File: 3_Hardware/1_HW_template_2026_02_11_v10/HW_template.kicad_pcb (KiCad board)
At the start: 2 copper layers, 63.5 x 118.1 mm, 47 parts, among them P1 type="R" model="Conn_01x32_Fe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, P2 type="R" model="Conn_01x32_Fe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, Q1 BSS316N, SW1 type="R" model="SW_Push" lib=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, U1 LD1117S33TR_SOT223, U2 SiP32508, U3 MCP6002/MCP6272, U4 MCP6002/MCP6272, Y1 Radar K-LC5-RFB-00C, Y2 OpenLog

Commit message: layout template
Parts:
- removed LED3: LEDred, LED_SMD:LED_1206_3216Metric_Pad1.42x1.75mm_HandSolder
- removed Q1: BSS316N, Package_TO_SOT_SMD:SOT-23
- removed R22: 100k, Resistor_SMD:R_0805_2012Metric_Pad1.20x1.40mm_HandSolder
- removed SD1: SD103AWS, Diode_SMD:D_SOD-323_HandSoldering
- removed SD2: SS13L, Diode_SMD:D_SMA
- removed SW1: type="R" model="SW_Push" lib="", Button_Switch_SMD:SW_SPST_PTS645
- removed the TP4 at (128.5, 42.5)
- added BZ1: Buzzer_Piezo, Buzzer_Beeper:Buzzer_Murata_PKMCS0909E, F.Cu at (175.2, 153.5)
- added C10: 100u, Capacitor_SMD:C_1210_3225Metric_Pad1.33x2.70mm_HandSolder, F.Cu at (137.3, 172.7)
- added C11: 4n7, Capacitor_SMD:C_0603_1608Metric_Pad1.08x0.95mm_HandSolder, F.Cu at (138.8, 176.2)
- added C12: 100u, Capacitor_SMD:C_1210_3225Metric_Pad1.33x2.70mm_HandSolder, F.Cu at (150.5, 174.0)
- added C13: 4n7, Capacitor_SMD:C_0603_1608Metric_Pad1.08x0.95mm_HandSolder, F.Cu at (149.0, 177.5)
- added C14: 10u, Capacitor_SMD:C_0603_1608Metric_Pad1.08x0.95mm_HandSolder, F.Cu at (154.0, 177.5)
- added C15: 10u, Capacitor_SMD:C_0805_2012Metric_Pad1.18x1.45mm_HandSolder, F.Cu at (172.0, 70.6)
- added C16: 100n, Capacitor_SMD:C_0805_2012Metric_Pad1.18x1.45mm_HandSolder, F.Cu at (141.0, 130.4)
- added C17: 10u, Capacitor_SMD:C_0805_2012Metric_Pad1.18x1.45mm_HandSolder, F.Cu at (134.5, 136.4)
- added C18: 100n, Capacitor_SMD:C_0805_2012Metric_Pad1.18x1.45mm_HandSolder, F.Cu at (172.0, 79.6)
- added C19: 100n, Capacitor_SMD:C_0805_2012Metric_Pad1.18x1.45mm_HandSolder, F.Cu at (142.0, 139.4)
- added C20: 10u, Capacitor_SMD:C_0805_2012Metric_Pad1.18x1.45mm_HandSolder, F.Cu at (158.0, 127.6)
- added C21: 100n, Capacitor_SMD:C_0805_2012Metric_Pad1.18x1.45mm_HandSolder, F.Cu at (156.0, 127.6)
- added C22: 10uF, Capacitor_SMD:C_0805_2012Metric_Pad1.18x1.45mm_HandSolder, F.Cu at (168.0, 127.6)
- added C23: 100n, Capacitor_SMD:C_0805_2012Metric_Pad1.18x1.45mm_HandSolder, F.Cu at (170.0, 127.6)
- added C7: 10u, Capacitor_SMD:C_0603_1608Metric_Pad1.08x0.95mm_HandSolder, F.Cu at (154.0, 158.0)
- added C8: 100n, Capacitor_SMD:C_0603_1608Metric_Pad1.08x0.95mm_HandSolder, F.Cu at (145.3, 174.2)
- added C9: 10u, Capacitor_SMD:C_0603_1608Metric_Pad1.08x0.95mm_HandSolder, F.Cu at (133.3, 177.7)
- added JP1: SolderJumper_2_Open, Jumper:SolderJumper-2_P1.3mm_Open_RoundedPad1.0x1.5mm, F.Cu at (157.8, 154.6)
- added JP2: SolderJumper_2_Open, Jumper:SolderJumper-2_P1.3mm_Open_RoundedPad1.0x1.5mm, F.Cu at (157.7, 174.2)
- added JP3: SolderJumper_2_Open, Jumper:SolderJumper-2_P1.3mm_Open_RoundedPad1.0x1.5mm, F.Cu at (173.0, 134.8)
- added TP1: Channel1, TestPoint:TestPoint_Loop_D2.60mm_Drill1.6mm_Beaded, F.Cu at (160.5, 71.6)
- added TP5: ~, TestPoint:TestPoint_Loop_D2.60mm_Drill1.6mm_Beaded, F.Cu at (160.5, 81.7)
- added TP6: ~, TestPoint:TestPoint_Loop_D2.60mm_Drill1.6mm_Beaded, F.Cu at (146.0, 134.4)
- added TP7: ~, TestPoint:TestPoint_Loop_D2.60mm_Drill1.6mm_Beaded, F.Cu at (157.0, 134.6)
- added TP8: ~, TestPoint:TestPoint_Loop_D2.60mm_Drill1.6mm_Beaded, F.Cu at (169.0, 134.8)
- C1: value 100uF -> 100n; footprint Capacitor_SMD:C_1206_3216Metric_Pad1.33x1.80mm_HandSolder -> Capacitor_SMD:C_0603_1608Metric_Pad1.08x0.95mm_HandSolder
- C2: value 10uF -> 10u; footprint Capacitor_SMD:C_0805_2012Metric_Pad1.18x1.45mm_HandSolder -> Capacitor_SMD:C_0603_1608Metric_Pad1.08x0.95mm_HandSolder
- C3: value 10uF -> 100u; footprint Capacitor_SMD:C_0805_2012Metric_Pad1.18x1.45mm_HandSolder -> Capacitor_SMD:C_1210_3225Metric_Pad1.33x2.70mm_HandSolder
- C4, C6: value 100n -> 4n7; footprint Capacitor_SMD:C_0805_2012Metric_Pad1.18x1.45mm_HandSolder -> Capacitor_SMD:C_0603_1608Metric_Pad1.08x0.95mm_HandSolder
- C5: value 100n -> 100u; footprint Capacitor_SMD:C_0805_2012Metric_Pad1.18x1.45mm_HandSolder -> Capacitor_SMD:C_1210_3225Metric_Pad1.33x2.70mm_HandSolder
- LED1: value LEDblue -> LEDred; footprint LED_SMD:LED_1206_3216Metric_Pad1.42x1.75mm_HandSolder -> LED_SMD:LED_0603_1608Metric_Pad1.05x0.95mm_HandSolder
- LED2: value LEDgreen -> LEDred; footprint LED_SMD:LED_1206_3216Metric_Pad1.42x1.75mm_HandSolder -> LED_SMD:LED_0603_1608Metric_Pad1.05x0.95mm_HandSolder
- R1: value 0R -> 100k; footprint Resistor_SMD:R_0805_2012Metric_Pad1.20x1.40mm_HandSolder -> Resistor_SMD:R_0603_1608Metric_Pad0.98x0.95mm_HandSolder
- R10, R14, R3: value 1k -> 10k; footprint Resistor_SMD:R_0805_2012Metric_Pad1.20x1.40mm_HandSolder -> Resistor_SMD:R_0603_1608Metric_Pad0.98x0.95mm_HandSolder
- R11, R2: value 1k -> 1M; footprint Resistor_SMD:R_0805_2012Metric_Pad1.20x1.40mm_HandSolder -> Resistor_SMD:R_0603_1608Metric_Pad0.98x0.95mm_HandSolder
- R12: footprint Resistor_SMD:R_0805_2012Metric_Pad1.20x1.40mm_HandSolder -> Resistor_SMD:R_0603_1608Metric_Pad0.98x0.95mm_HandSolder
- R13: value 12k -> 1k; footprint Resistor_SMD:R_0805_2012Metric_Pad1.20x1.40mm_HandSolder -> Resistor_SMD:R_0603_1608Metric_Pad0.98x0.95mm_HandSolder
- R15: value 1k -> 220R
- R16: value 22 -> 1k; footprint Resistor_SMD:R_0805_2012Metric_Pad1.20x1.40mm_HandSolder -> Resistor_SMD:R_0603_1608Metric_Pad0.98x0.95mm_HandSolder
- R17: value 47 -> 1k; footprint Resistor_SMD:R_0805_2012Metric_Pad1.20x1.40mm_HandSolder -> Resistor_SMD:R_0603_1608Metric_Pad0.98x0.95mm_HandSolder
- R18, R19: value 100 -> 10k
- R20: value 100 -> 100k
- R21: value 10 -> 1k
- R4: value ~ -> 1M; footprint Resistor_SMD:R_0805_2012Metric_Pad1.20x1.40mm_HandSolder -> Resistor_SMD:R_0603_1608Metric_Pad0.98x0.95mm_HandSolder
- R5, R7: value ~ -> 10k; footprint Resistor_SMD:R_0805_2012Metric_Pad1.20x1.40mm_HandSolder -> Resistor_SMD:R_0603_1608Metric_Pad0.98x0.95mm_HandSolder
- R6: value ~ -> 1k; footprint Resistor_SMD:R_0805_2012Metric_Pad1.20x1.40mm_HandSolder -> Resistor_SMD:R_0603_1608Metric_Pad0.98x0.95mm_HandSolder
- R8: value 10k -> 100k; footprint Resistor_SMD:R_0805_2012Metric_Pad1.20x1.40mm_HandSolder -> Resistor_SMD:R_0603_1608Metric_Pad0.98x0.95mm_HandSolder
- R9: value 12k -> 1M; footprint Resistor_SMD:R_0805_2012Metric_Pad1.20x1.40mm_HandSolder -> Resistor_SMD:R_0603_1608Metric_Pad0.98x0.95mm_HandSolder
- U1: value LD1117S33TR_SOT223 -> MCP6002-xSN; footprint Package_TO_SOT_SMD:SOT-223-3_TabPin2 -> Package_SO:SOIC-8_3.9x4.9mm_P1.27mm
- U2: value SiP32508 -> MCP6002-xSN; footprint Package_TO_SOT_SMD:TSOT-23-6_HandSoldering -> Package_SO:SOIC-8_3.9x4.9mm_P1.27mm
- U3: value MCP6002/MCP6272 -> MCP6002-xSN
- U4: value MCP6002/MCP6272 -> LD1117S33TR_SOT223; footprint Package_SO:SOIC-8_3.9x4.9mm_P1.27mm -> Package_TO_SOT_SMD:SOT-223-3_TabPin2
- Y1: value Radar K-LC5-RFB-00C -> OpenLog; footprint HW_template:Radar_K-LC5 -> Connector_PinHeader_2.54mm:PinHeader_1x06_P2.54mm_Vertical
- Y2: value OpenLog -> Radar K-LC5-RFB-00C; footprint Connector_PinHeader_2.54mm:PinHeader_1x06_P2.54mm_Vertical -> HW_template:Radar_K-LC5
- moved R1 132.2 mm to (133.6, 159.5), turned to 180 degrees
- moved U2 131.9 mm to (143.8, 177.8)
- moved U1 128.6 mm to (144.0, 158.1)
- moved R2 126.8 mm to (137.6, 156.5), turned to -90 degrees
- moved R8 126.8 mm to (133.3, 179.2), turned to 180 degrees
- moved C1 126.7 mm to (145.6, 154.5), turned to 180 degrees
- moved R12 125.2 mm to (152.0, 177.5), turned to 90 degrees
- moved R4 125.1 mm to (150.6, 158.0), turned to -90 degrees
- moved R3 123.7 mm to (136.1, 156.5), turned to 90 degrees
- moved R5 122.7 mm to (152.1, 158.0), turned to 90 degrees
- moved C2 121.6 mm to (133.6, 158.0), turned to 180 degrees
- moved R9 121.5 mm to (137.3, 176.2), turned to -90 degrees
- moved R17 120.0 mm to (197.5, 137.6), turned to 90 degrees
- moved R16 119.9 mm to (191.0, 137.6), turned to 90 degrees
- moved R11 119.7 mm to (150.5, 177.5), turned to -90 degrees
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- renumbered TP1 to TP2, TP2 to TP4
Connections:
- C1 pad 1: +5V -> 3V3_INT
- C2 pad 1: Net-(U1-VI) -> Net-(U1A-+)
- C2 pad 2: GND -> IF_Q
- C3 pad 1: Net-(U1-VO) -> Net-(C3-Pad1)
- C4 pad 1: 3V3_INT -> Net-(U1B-+)
- C4 pad 2: GND -> Net-(U1A--)
- C5 pad 1: 3V3_INT -> Net-(C5-Pad1)
- C6 pad 1: 3V3_INT -> Net-(JP1-A)
- C6 pad 2: GND -> Net-(U1B--)
- R1 pad 1: Net-(U1-VO) -> Net-(U1A-+)
- R1 pad 2: 3V3_INT -> Vref
- R10 pad 1: Net-(U3A--) -> Net-(U2A--)
- R10 pad 2: GND -> Net-(C10-Pad1)
- R11 pad 1: Net-(U3B--) -> Net-(JP2-A)
- R11 pad 2: GND -> Net-(U2B--)
- R12 pad 1: Net-(U4B-+) -> Net-(U2B--)
- R12 pad 2: Net-(U4A--) -> Net-(C12-Pad1)
- R13 pad 1: /channel2/out -> Net-(JP2-A)
- R13 pad 2: Net-(U4B--) -> PC1
- R14 pad 1: Net-(U4A--) -> PC1
- R15 pad 1: Net-(U4B--) -> Net-(BZ1-+)
- R15 pad 2: GND -> Buzz
- R16 pad 1: Enable -> D0
- R17 pad 1: Enable -> D1
- R18 pad 1: Enable -> 3V3_INT
- R18 pad 2: Net-(LED3-A) -> Net-(U3A-+)
- R19 pad 1: Enable -> Net-(U3A-+)
- R19 pad 2: Net-(SD1-A) -> GND
- R2 pad 1: Net-(U1-VI) -> Net-(U1B-+)
- R2 pad 2: GND -> Net-(U1A--)
- R20 pad 1: Enable -> PA5
- R20 pad 2: Net-(SD2-A) -> Net-(U3B-+)
- R21 pad 1: +5V -> Net-(JP3-A)
- R21 pad 2: Net-(Q1-D) -> GND
- R3 pad 1: Net-(U1-VO) -> Net-(U1A--)
- R3 pad 2: GND -> Net-(C3-Pad1)
- R4 pad 1: /channel1/out -> Net-(JP1-A)
- R4 pad 2: PC1 -> Net-(U1B--)
- R5 pad 1: PC1 -> Net-(U1B--)
- R5 pad 2: GND -> Net-(C5-Pad1)
- R6 pad 1: /channel2/out -> Net-(JP1-A)
- R8 pad 1: Net-(U3B-+) -> Net-(U2A-+)
- R8 pad 2: Net-(U3A--) -> Vref
- R9 pad 1: /channel1/out -> Net-(U2B-+)
- R9 pad 2: Net-(U3B--) -> Net-(U2A--)
- TP3 pad 1: GND -> PC3
- U1 pad 1: GND -> Net-(U1B-+)
- U1 pad 2: Net-(U1-VO) -> Net-(U1A--)
- U1 pad 3: Net-(U1-VI) -> Net-(U1A-+)
- U2 pad 1: Net-(U1-VI) -> Net-(U2B-+)
- U2 pad 2: Net-(U1-VI) -> Net-(U2A--)
- U2 pad 3: Enable -> Net-(U2A-+)
- U2 pad 5: +5V -> Net-(U2B-+)
- U2 pad 6: +5V -> Net-(U2B--)
- U3 pad 1: Net-(U3B-+) -> Vref
- U3 pad 2: Net-(U3A--) -> Vref
- U3 pad 3: /channel1/in -> Net-(U3A-+)
- U3 pad 6: Net-(U3B--) -> /Analog/VCO_in
- U3 pad 7: /channel1/out -> /Analog/VCO_in
- U4 pad 1: Net-(U4B-+) -> GND
- U4 pad 2: Net-(U4A--) -> Net-(JP3-A)
- U4 pad 3: /channel2/in -> +5V
- Y1 pad 1: unconnected-(Y1-IF_Q-Pad1) -> PE6
- Y1 pad 2: 3V3_INT -> PA9
- Y1 pad 3: unconnected-(Y1-IF_I-Pad3) -> PA10
- Y1 pad 4: GND -> +5V
- Y1 pad 5: PA5 -> GND
- Y2 pad 1: PE6 -> IF_Q
- Y2 pad 2: PA9 -> 3V3_INT
- Y2 pad 3: PA10 -> IF_I
- Y2 pad 4: +5V -> GND
- Y2 pad 5: GND -> /Analog/VCO_in
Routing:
- net Net-(JP3-A): track 0.00 -> 27.8 mm
- net Net-(JP2-A): track 0.00 -> 17.9 mm
- net Net-(JP1-A): track 0.00 -> 17.8 mm
- net Net-(U2B-+): track 0.00 -> 12.0 mm
- net Net-(U1B-+): track 0.00 -> 12.0 mm
- net +5V: track 0.00 -> 11.4 mm
- net Net-(U2A-+): track 0.00 -> 10.9 mm
- net Net-(U1A-+): track 0.00 -> 10.9 mm
- net /Analog/VCO_in: track 0.00 -> 7.51 mm
- net Net-(U3A-+): track 0.00 -> 6.68 mm
- net Net-(U2B--): track 0.00 -> 5.78 mm
- net 3V3_INT: track 0.00 -> 5.61 mm
- net Net-(U1B--): track 0.00 -> 5.61 mm
- net Net-(U2A--): track 0.00 -> 5.58 mm
- net Net-(U1A--): track 0.00 -> 5.58 mm
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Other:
- board text added: "+3V3"
- board text added: "+5V"
- board text added: "CH1 - IF_Q"
- board text added: "CH2 - IF_I"
- board text added: "D0 D1"
- board text added: "Debug"
- board text added: "IN"
- board text added: "OUT"
- board text added: "VREF"
- board text added: "bzzzzz"
- board text added: "err0: 0 0 err1: 0 1 err2: 1 0 err3: 1 1"

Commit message: added AD8232
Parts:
- C15, C18: footprint Capacitor_SMD:C_0805_2012Metric_Pad1.18x1.45mm_HandSolder -> Capacitor_SMD:C_0603_1608Metric_Pad1.08x0.95mm_HandSolder
- moved C15 4.42 mm to (174.1, 74.5)
- moved C18 3.37 mm to (174.1, 77.0)

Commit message: added datasheet and started layout
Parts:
- added C25: 1n, Capacitor_SMD:C_0603_1608Metric_Pad1.08x0.95mm_HandSolder, F.Cu at (145.4, 119.4)
- added C26: 330n, Capacitor_SMD:C_0603_1608Metric_Pad1.08x0.95mm_HandSolder, F.Cu at (145.4, 121.9)
- added C27: 330n, Capacitor_SMD:C_0603_1608Metric_Pad1.08x0.95mm_HandSolder, F.Cu at (145.4, 124.5)
- added C28: 100n, Capacitor_SMD:C_0603_1608Metric_Pad1.08x0.95mm_HandSolder, F.Cu at (145.4, 127.0)
- added C29: 100n, Capacitor_SMD:C_0603_1608Metric_Pad1.08x0.95mm_HandSolder, F.Cu at (145.4, 129.5)
- added C30: 1n5, Capacitor_SMD:C_0603_1608Metric_Pad1.08x0.95mm_HandSolder, F.Cu at (145.4, 132.0)
- added C31: 10n, Capacitor_SMD:C_0603_1608Metric_Pad1.08x0.95mm_HandSolder, F.Cu at (145.4, 134.5)
- added LA1: MountingHole_Pad, TestPoint:TestPoint_Loop_D2.60mm_Drill1.6mm_Beaded, F.Cu at (150.1, 120.7)
- added R23: 10M, Resistor_SMD:R_0805_2012Metric_Pad1.20x1.40mm_HandSolder, F.Cu at (155.0, 119.7)
- added R24: 10M, Resistor_SMD:R_0805_2012Metric_Pad1.20x1.40mm_HandSolder, F.Cu at (155.0, 122.6)
- added R25: 10M, Resistor_SMD:R_0805_2012Metric_Pad1.20x1.40mm_HandSolder, F.Cu at (155.0, 125.5)
- added R28: 1M4, Resistor_SMD:R_0805_2012Metric_Pad1.20x1.40mm_HandSolder, F.Cu at (155.0, 128.5)
- added R29: 180k, Resistor_SMD:R_0805_2012Metric_Pad1.20x1.40mm_HandSolder, F.Cu at (155.0, 131.4)
- added R30: 360k, Resistor_SMD:R_0805_2012Metric_Pad1.20x1.40mm_HandSolder, F.Cu at (159.8, 119.7)
- added R31: 100k, Resistor_SMD:R_0805_2012Metric_Pad1.20x1.40mm_HandSolder, F.Cu at (159.8, 122.6)
- added R34: 180k, Resistor_SMD:R_0805_2012Metric_Pad1.20x1.40mm_HandSolder, F.Cu at (159.8, 125.5)
- added R35: 10M, Resistor_SMD:R_0805_2012Metric_Pad1.20x1.40mm_HandSolder, F.Cu at (159.8, 128.5)
- added R36: 10M, Resistor_SMD:R_0805_2012Metric_Pad1.20x1.40mm_HandSolder, F.Cu at (159.8, 131.4)
- added R37: 10M, Resistor_SMD:R_0805_2012Metric_Pad1.20x1.40mm_HandSolder, F.Cu at (164.5, 119.7)
- added R38: 1M, Resistor_SMD:R_0805_2012Metric_Pad1.20x1.40mm_HandSolder, F.Cu at (164.5, 122.6)
- added R39: 1M, Resistor_SMD:R_0805_2012Metric_Pad1.20x1.40mm_HandSolder, F.Cu at (164.5, 125.5)
- added R40: 1M, Resistor_SMD:R_0805_2012Metric_Pad1.20x1.40mm_HandSolder, F.Cu at (164.5, 128.5)
- added RA1: MountingHole_Pad, TestPoint:TestPoint_Loop_D2.60mm_Drill1.6mm_Beaded, F.Cu at (150.1, 125.8)
- added RL1: MountingHole_Pad, TestPoint:TestPoint_Loop_D2.60mm_Drill1.6mm_Beaded, F.Cu at (150.1, 130.8)
- moved JP3 119.9 mm to (53.4, 127.8), turned to 180 degrees
- moved C18 117.8 mm to (57.0, 89.0), turned to 90 degrees
- moved C15 116.5 mm to (58.5, 89.0), turned to 90 degrees
- moved TP8 116.2 mm to (53.4, 123.8), turned to 180 degrees
- moved R21 112.0 mm to (60.5, 127.3), turned to 0 degrees
- moved C23 109.6 mm to (60.5, 124.8), turned to 0 degrees
- moved Y2 107.8 mm to (62.0, 94.1), turned to 180 degrees
- moved C22 107.6 mm to (60.5, 122.8), turned to 0 degrees
- moved TP7 106.0 mm to (53.5, 111.8), turned to 180 degrees
- moved U4 105.8 mm to (58.0, 117.8), turned to 180 degrees
- moved U2 100.2 mm to (79.3, 101.1)
- moved C10 100.2 mm to (72.8, 96.0)
- moved C11 100.2 mm to (74.3, 99.5)
- moved C12 100.2 mm to (86.0, 97.3)
- moved C13 100.2 mm to (84.5, 100.8)
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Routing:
- added copper zone on In2.Cu, net 3V3_INT
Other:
- copper layers 2 -> 4
- board text added: "ET.PM4 = Radar-Sensor perritho - grebnbog"
- board text removed: "Sensor-Board: HW template for ET.PM4 = Radar-Sensor (c) renn@zhaw.ch January 2026"
- board text removed: "The 32 pin connectors are on the bottom side!"
- board text removed: "The GND plates have already been added. Press B to fill, CTRL + B to unfill all plates/zones."

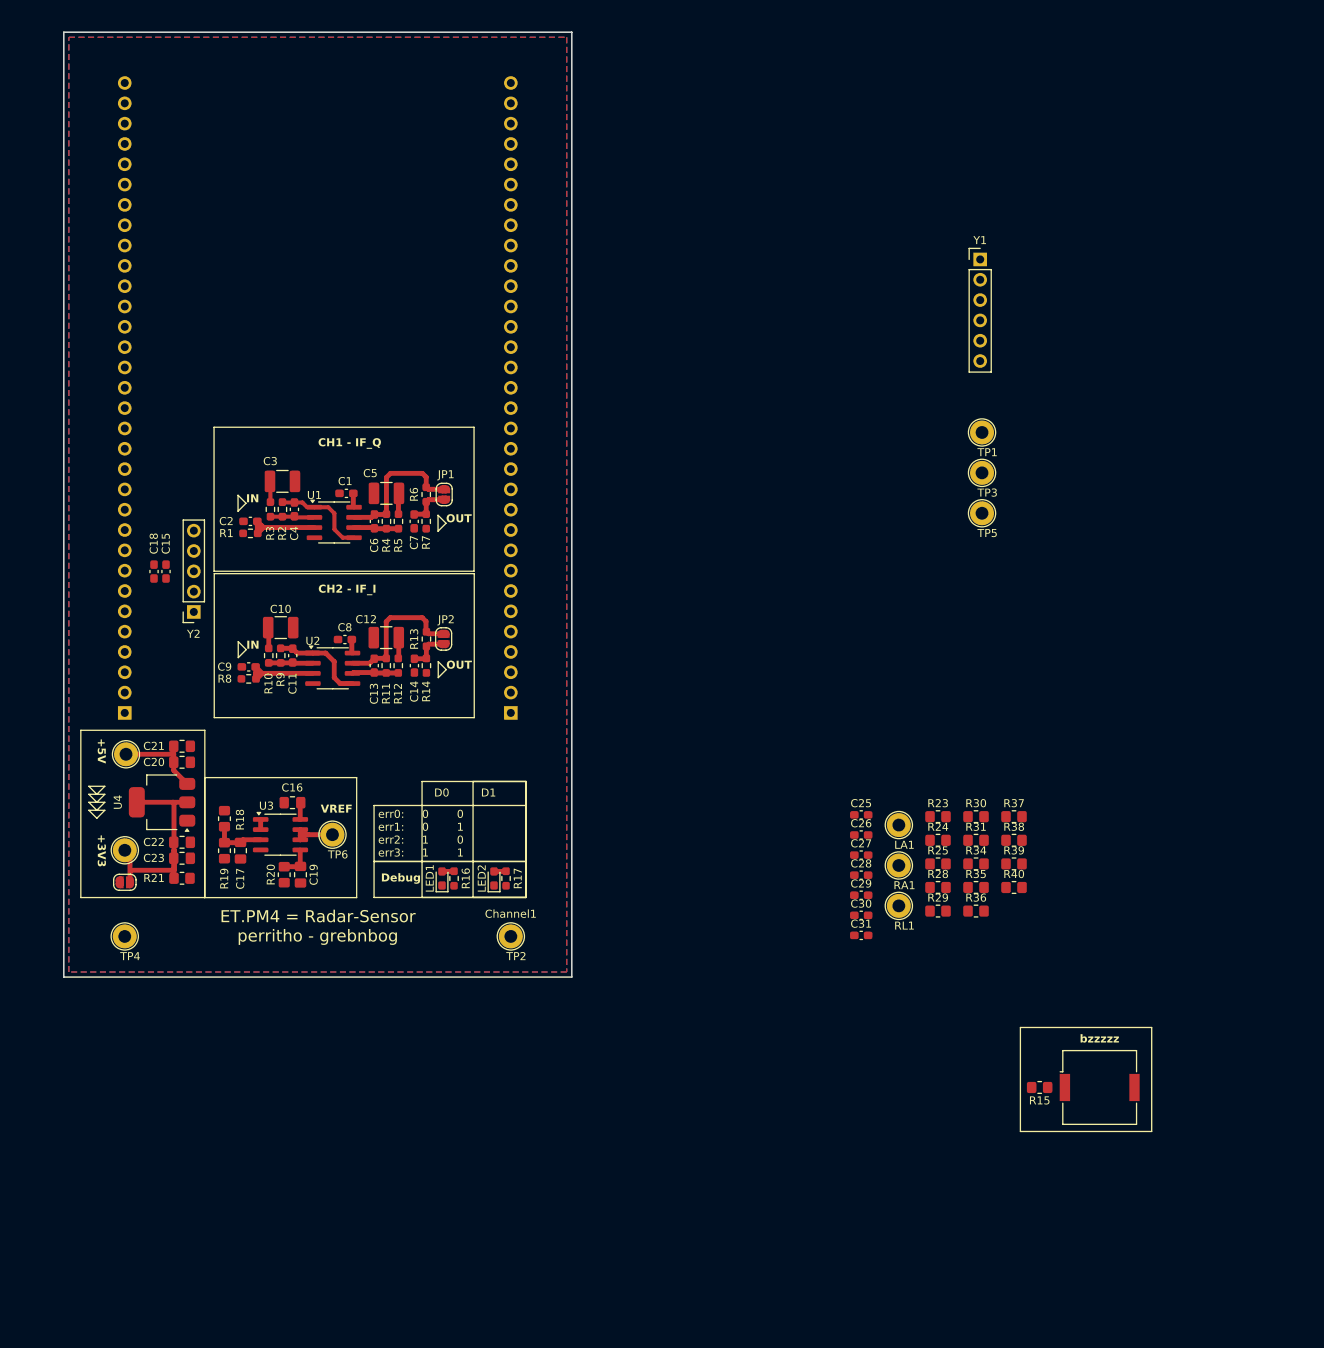
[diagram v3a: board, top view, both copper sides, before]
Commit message: updated layout
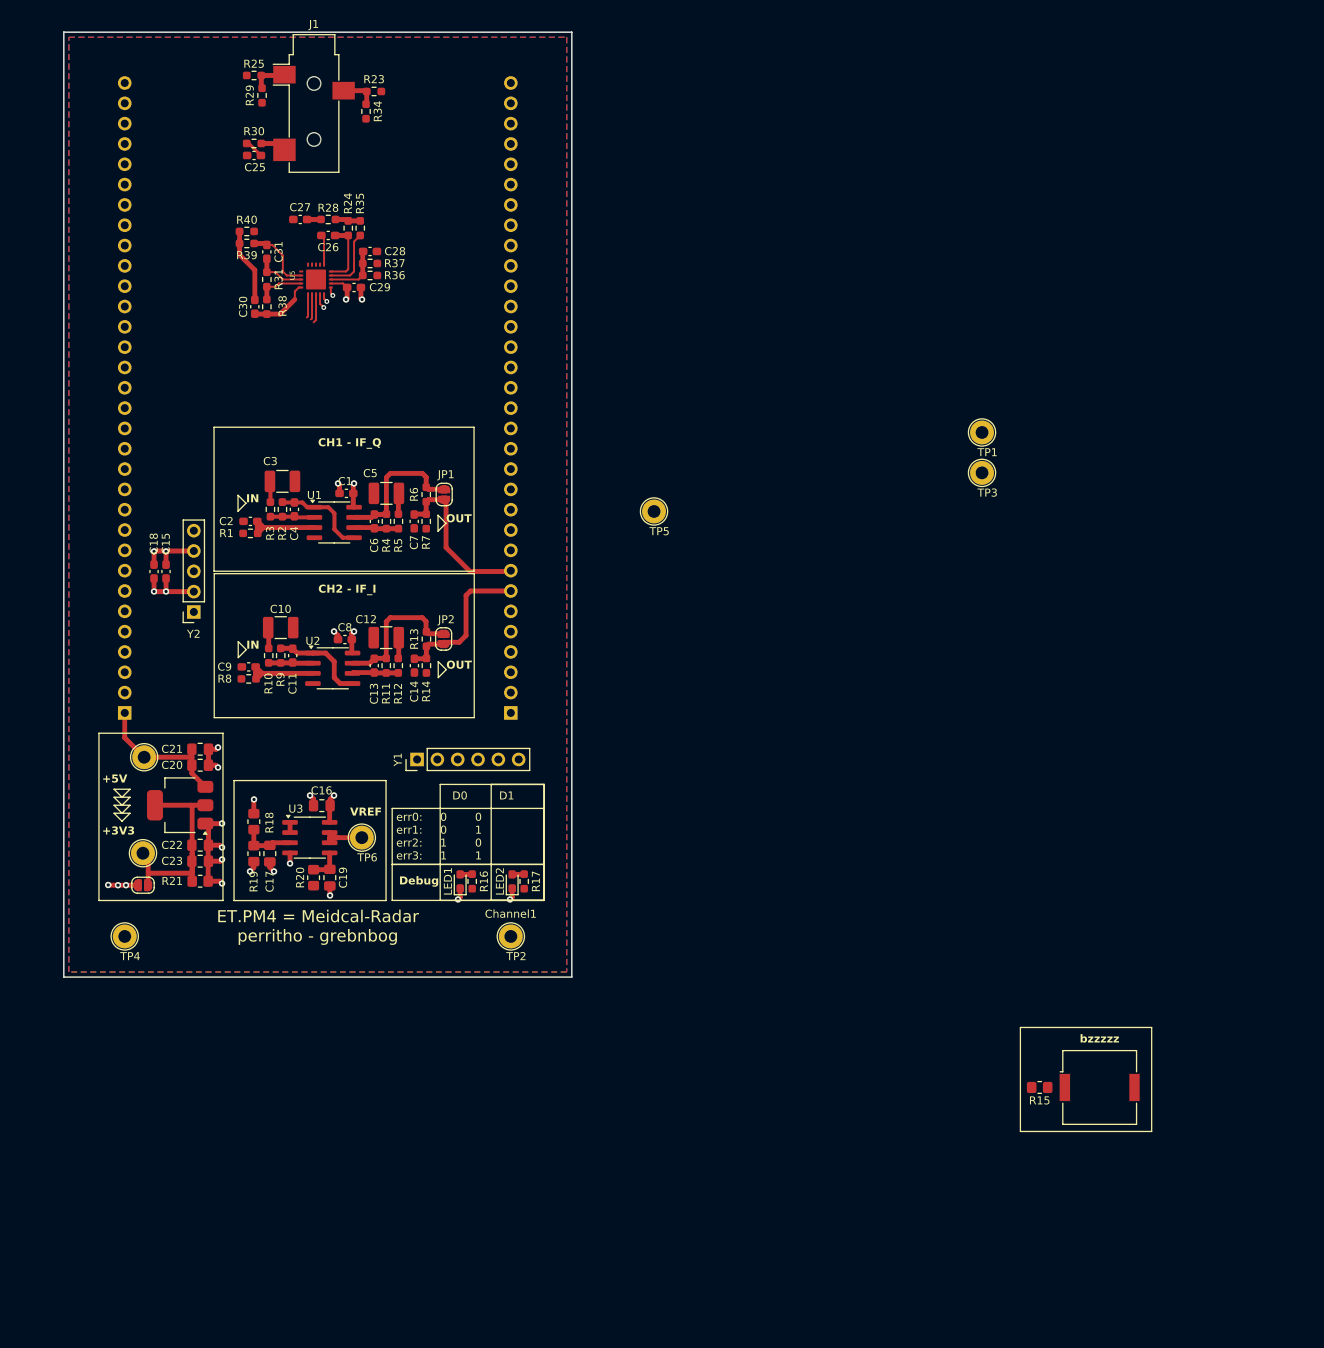
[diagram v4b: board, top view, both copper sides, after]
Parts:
- removed LA1, RA1, RL1: MountingHole_Pad, TestPoint:TestPoint_Loop_D2.60mm_Drill1.6mm_Beaded
- added J1: AudioJack3, Connector_Audio:Jack_3.5mm_CUI_SJ-3523-SMT_Horizontal, F.Cu at (77.0, 30.5)
- added U5: AD8232ACPZ-R7, AD8232:LFCSP_20, F.Cu at (77.2, 52.5)
- R23, R24, R25, R28, R29, R30, R31, R34, R35, R36, R37, R38, R39, R40: footprint Resistor_SMD:R_0805_2012Metric_Pad1.20x1.40mm_HandSolder -> Resistor_SMD:R_0603_1608Metric_Pad0.98x0.95mm_HandSolder
- moved R29 132.4 mm to (70.5, 29.5), turned to -90 degrees
- moved R25 130.5 mm to (69.5, 27.0)
- moved R40 126.2 mm to (68.6, 46.5)
- moved R30 123.4 mm to (69.5, 35.5), turned to 180 degrees
- moved R39 123.3 mm to (68.6, 48.0)
- moved R34 121.1 mm to (83.5, 31.5), turned to -90 degrees
- moved R23 114.8 mm to (84.5, 29.0), turned to 180 degrees
- moved R38 114.8 mm to (71.1, 55.9), turned to -90 degrees
- moved C31 113.2 mm to (71.1, 49.0), turned to 90 degrees
- moved R28 113.1 mm to (78.8, 45.0)
- moved R31 113.0 mm to (71.1, 52.5), turned to -90 degrees
- moved R35 112.8 mm to (82.8, 46.1), turned to 90 degrees
- moved C25 112.1 mm to (69.5, 37.0)
- moved R36 109.8 mm to (84.0, 52.0), turned to 180 degrees
- moved C30 107.4 mm to (69.6, 55.9), turned to 90 degrees
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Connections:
- C31 pad 1: Net-(U5-REFOUT) -> REFOUT
- R31 pad 1: Net-(U5-REFOUT) -> REFOUT
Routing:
- net GND: track 0.00 -> 44.6 mm, vias 0 -> 20
- net 3V3_INT: track 5.61 -> 28.2 mm, vias 0 -> 11
- net PC3: track 5.41 -> 20.9 mm
- net PC1: track 5.29 -> 19.5 mm
- net Net-(C30-Pad2): track 0.00 -> 9.34 mm
- net Net-(U5-OPAMP+): track 0.00 -> 8.72 mm
- net Net-(U5-HPSENSE): track 0.00 -> 8.15 mm
- net Net-(U5-IAOUT): track 0.00 -> 7.93 mm
- net /ECG/sig_out: track 0.00 -> 7.78 mm
- net Net-(U5-REFIN): track 0.00 -> 7.22 mm
- net +5V: track 11.4 -> 17.9 mm
- net REFOUT: track 0.00 -> 6.35 mm
- net Net-(U5-OPAMP-): track 0.00 -> 6.06 mm
- net Net-(J1-PadS): track 0.00 -> 4.95 mm
- net Net-(J1-PadR): track 0.00 -> 4.55 mm
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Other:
- board text added: "ET.PM4 = Meidcal-Radar perritho - grebnbog"
- board text removed: "ET.PM4 = Radar-Sensor perritho - grebnbog"
